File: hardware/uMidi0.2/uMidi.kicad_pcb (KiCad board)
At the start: 2 copper layers, 66 x 40.6 mm, 59 parts, among them CON1 USB-MINI-B, IC1 ATXMEGA128A4U-M, IC2 74LS14, IC3 LT1129CST-3.3, IC4 6N138, P1 MIDI In, P2 MIDI Thru, P3 MIDI T/O, P4 MIDI Out, P5 5..12 V, P6 PDI, P7 GPIO1, P8 GPIO2, P9 GPIO2

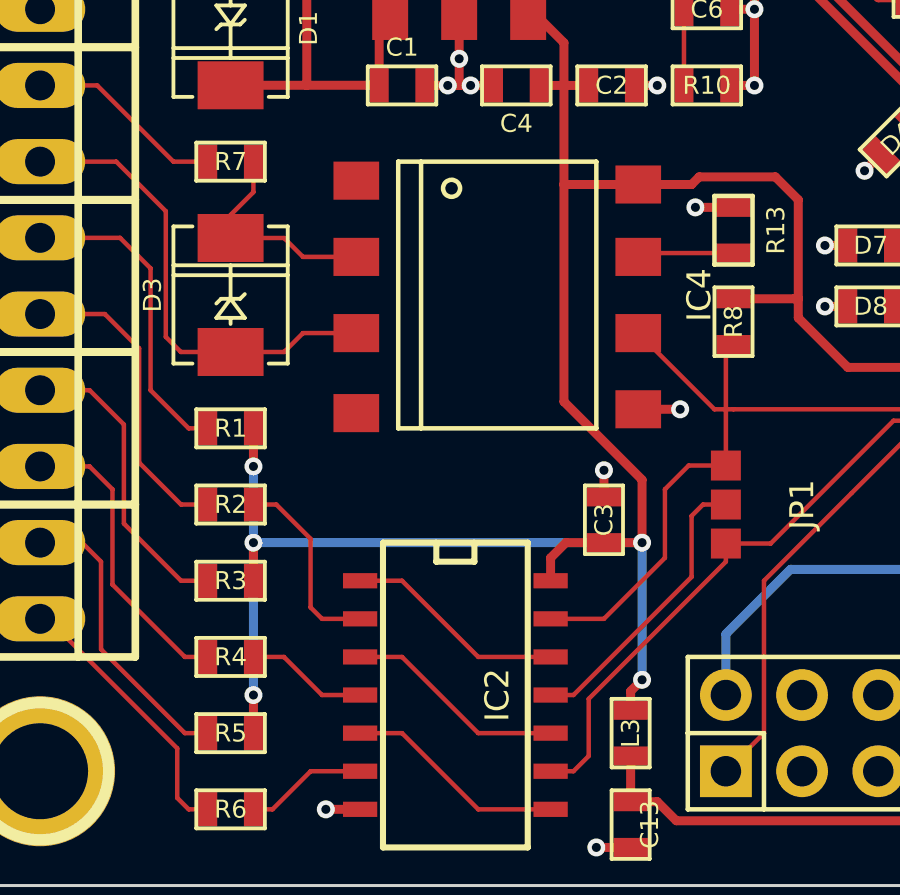
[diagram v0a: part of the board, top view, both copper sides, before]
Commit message: Modify placement of C3
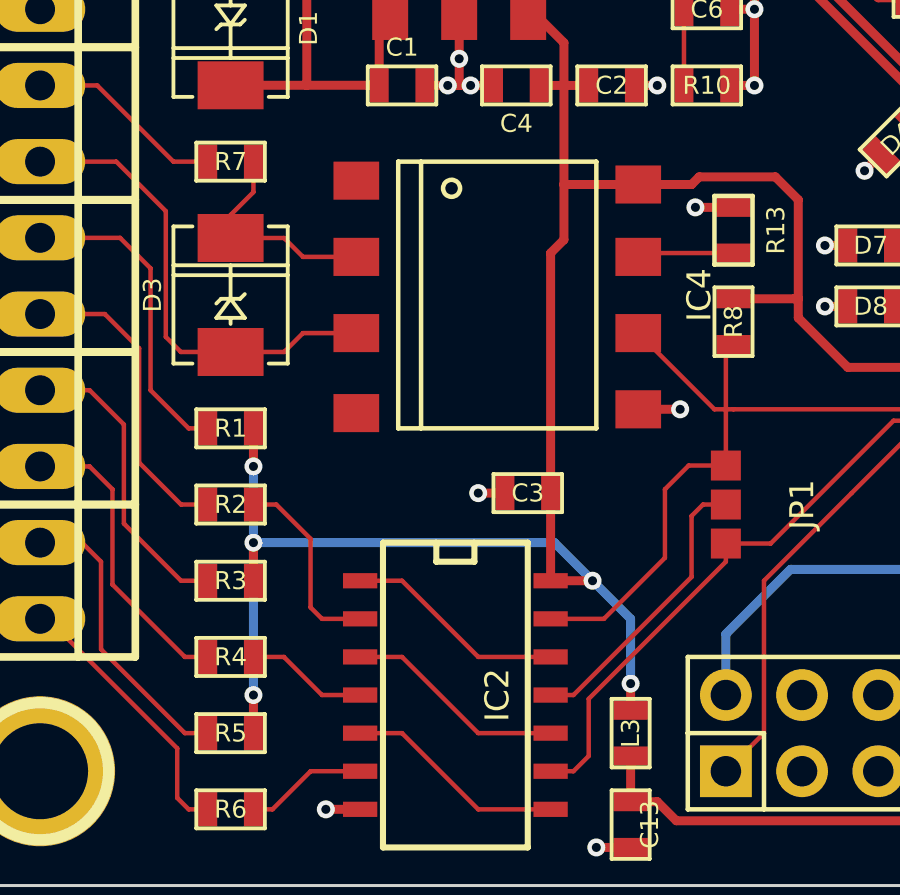
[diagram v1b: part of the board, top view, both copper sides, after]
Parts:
- moved C3 2.69 mm to (87.4, 150.7), turned to 180 degrees
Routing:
- net +3.3V: track 75.4 -> 71.2 mm
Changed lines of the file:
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@@
     (links 155)
     (no_connects 1)
-    (area 64.280952 120.39205 138.793784 166.53905)
+    (area 64.265952 120.77 137.108095 166.2406)
     (thickness 1.6)
     (drawings 4)
-    (tracks 477)
+    (tracks 475)
     (zones 0)
     (modules 59)
@@
   )
   (module SMD_Packages:SMD-0603 (layer F.Cu)
-    (at 89.916 151.638 90)
-    (attr smd)
-    (fp_text reference C3 (at 0 0 90) (layer F.SilkS)
-      (effects (font (size 0.6 0.6) (thickness 0.1143)))
-    )
-    (fp_text value 100n (at 0 0 90) (layer F.SilkS) hide
-      (effects (font (size 0.6 0.6) (thickness 0.1143)))
-    )
-    (fp_line (start -1.143 -0.635) (end 1.143 -0.635) (layer F.SilkS) (width 0.127))
-    (fp_line (start 1.143 -0.635) (end 1.143 0.635) (layer F.SilkS) (width 0.127))
-    (fp_line (start 1.143 0.635) (end -1.143 0.635) (layer F.SilkS) (width 0.127))
-    (fp_line (start -1.143 0.635) (end -1.143 -0.635) (layer F.SilkS) (width 0.127))
-    (pad 1 smd rect (at -0.762 0 90) (size 0.635 1.143) (layers F.Cu F.Paste F.Mask)
+    (at 87.376 150.749 180)
+    (attr smd)
+    (fp_text reference C3 (at 0 0 180) (layer F.SilkS)
+      (effects (font (size 0.6 0.6) (thickness 0.1143)))
+    )
+    (fp_text value 100n (at 0 0 180) (layer F.SilkS) hide
+      (effects (font (size 0.6 0.6) (thickness 0.1143)))
+    )
+    (fp_line (start -1.143 -0.635) (end 1.143 -0.635) (layer F.SilkS) (width 0.127))
+    (fp_line (start 1.143 -0.635) (end 1.143 0.635) (layer F.SilkS) (width 0.127))
+    (fp_line (start 1.143 0.635) (end -1.143 0.635) (layer F.SilkS) (width 0.127))
+    (fp_line (start -1.143 0.635) (end -1.143 -0.635) (layer F.SilkS) (width 0.127))
+    (pad 1 smd rect (at -0.762 0 180) (size 0.635 1.143) (layers F.Cu F.Paste F.Mask)
       (net 70 +3.3V))
-    (pad 2 smd rect (at 0.762 0 90) (size 0.635 1.143) (layers F.Cu F.Paste F.Mask)
+    (pad 2 smd rect (at 0.762 0 180) (size 0.635 1.143) (layers F.Cu F.Paste F.Mask)
       (net 2 GND))
     (model smd\resistors\R0603.wrl
@@
   (segment (start 82.41792 137.15492) (end 82.423 137.16) (width 0.3) (layer F.Cu) (net 1))
   (segment (start 82.588 134.747) (end 82.79 134.545) (width 0.3) (layer F.Cu) (net 1) (status 30))
+  (segment (start 86.614 150.749) (end 85.725 150.749) (width 0.3) (layer F.Cu) (net 2) (status 400000))
+  (via (at 85.725 150.749) (size 0.6) (layers F.Cu B.Cu) (net 2))
   (segment (start 90.805 162.56) (end 89.662 162.56) (width 0.3) (layer F.Cu) (net 2))
   (via (at 89.662 162.56) (size 0.6) (layers F.Cu B.Cu) (net 2))
@@
   (segment (start 89.154 128.905) (end 89.154 129.794) (width 0.3) (layer F.Cu) (net 2))
   (via (at 89.154 129.794) (size 0.6) (layers F.Cu B.Cu) (net 2))
-  (segment (start 89.916 150.876) (end 89.916 149.987) (width 0.3) (layer F.Cu) (net 2))
-  (via (at 89.916 149.987) (size 0.6) (layers F.Cu B.Cu) (net 2))
   (via (at 105.537 147.3835) (size 0.6) (layers F.Cu B.Cu) (net 2))
   (segment (start 105.537 146.558) (end 105.537 147.3835) (width 0.3) (layer F.Cu) (net 2))
@@
   (segment (start 101.092 142.494) (end 99.568 142.494) (width 0.15) (layer F.Cu) (net 68))
   (segment (start 101.092 144.526) (end 99.568 144.526) (width 0.15) (layer F.Cu) (net 69))
-  (segment (start 90.805 157.988) (end 90.805 157.353) (width 0.3) (layer F.Cu) (net 70))
-  (segment (start 91.186 156.972) (end 91.186 152.4) (width 0.3) (layer B.Cu) (net 70))
-  (via (at 91.186 156.972) (size 0.6) (layers F.Cu B.Cu) (net 70))
-  (segment (start 90.805 157.353) (end 91.186 156.972) (width 0.3) (layer F.Cu) (net 70))
-  (segment (start 89.916 152.4) (end 91.186 152.4) (width 0.3) (layer F.Cu) (net 70))
-  (segment (start 88.138 153.67) (end 88.138 152.908) (width 0.3) (layer F.Cu) (net 70))
-  (segment (start 88.646 152.4) (end 89.916 152.4) (width 0.3) (layer F.Cu) (net 70))
-  (segment (start 88.138 152.908) (end 88.646 152.4) (width 0.3) (layer F.Cu) (net 70))
+  (segment (start 89.535 153.67) (end 90.805 154.94) (width 0.3) (layer B.Cu) (net 70))
+  (segment (start 90.805 157.099) (end 90.805 157.988) (width 0.3) (layer F.Cu) (net 70) (status 800000))
+  (via (at 90.805 157.099) (size 0.6) (layers F.Cu B.Cu) (net 70))
+  (segment (start 90.805 154.94) (end 90.805 157.099) (width 0.3) (layer B.Cu) (net 70))
+  (segment (start 78.232 152.4) (end 88.265 152.4) (width 0.3) (layer B.Cu) (net 70))
+  (segment (start 89.535 153.67) (end 88.138 153.67) (width 0.3) (layer F.Cu) (net 70) (status 800000))
+  (via (at 89.535 153.67) (size 0.6) (layers F.Cu B.Cu) (net 70))
+  (segment (start 88.265 152.4) (end 89.535 153.67) (width 0.3) (layer B.Cu) (net 70))
+  (segment (start 88.138 150.749) (end 88.138 153.67) (width 0.3) (layer F.Cu) (net 70))
+  (segment (start 88.138 150.749) (end 88.138 142.748) (width 0.3) (layer F.Cu) (net 70))
+  (segment (start 88.5825 142.3035) (end 88.5825 140.462) (width 0.3) (layer F.Cu) (net 70))
+  (segment (start 88.138 142.748) (end 88.5825 142.3035) (width 0.3) (layer F.Cu) (net 70))
   (segment (start 78.232 153.67) (end 78.232 152.4) (width 0.3) (layer F.Cu) (net 70) (status 10))
   (segment (start 78.232 158.75) (end 78.232 157.48) (width 0.3) (layer F.Cu) (net 70))
@@
   (segment (start 78.232 149.86) (end 78.232 148.59) (width 0.3) (layer F.Cu) (net 70) (status 20))
   (via (at 78.232 149.86) (size 0.6) (layers F.Cu B.Cu) (net 70))
-  (via (at 91.186 152.4) (size 0.6) (layers F.Cu B.Cu) (net 70))
   (via (at 78.232 152.4) (size 0.6) (layers F.Cu B.Cu) (net 70))
   (segment (start 78.232 157.48) (end 78.232 152.4) (width 0.3) (layer B.Cu) (net 70))
   (segment (start 78.232 152.4) (end 78.232 149.86) (width 0.3) (layer B.Cu) (net 70))
-  (segment (start 91.186 152.4) (end 78.232 152.4) (width 0.3) (layer B.Cu) (net 70))
-  (segment (start 88.5825 140.462) (end 88.5825 147.701) (width 0.3) (layer F.Cu) (net 70))
   (segment (start 88.5825 137.16) (end 88.5825 140.462) (width 0.3) (layer F.Cu) (net 70))
   (segment (start 88.5825 135.7375) (end 88.5825 137.16) (width 0.3) (layer F.Cu) (net 70))
-  (segment (start 88.5825 147.701) (end 91.186 150.3045) (width 0.3) (layer F.Cu) (net 70))
-  (segment (start 91.186 150.3045) (end 91.186 152.4) (width 0.3) (layer F.Cu) (net 70))
-  (segment (start 91.186 152.4) (end 91.186 152.4) (width 0.3) (layer F.Cu) (net 70))
   (segment (start 87.39 134.545) (end 88.5825 135.7375) (width 0.3) (layer F.Cu) (net 70))
   (segment (start 88.519 137.16) (end 88.5825 137.16) (width 0.3) (layer F.Cu) (net 70))

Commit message: Placement silk screen
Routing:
- net GND: track 49.5 -> 50.4 mm, vias 25 -> 24

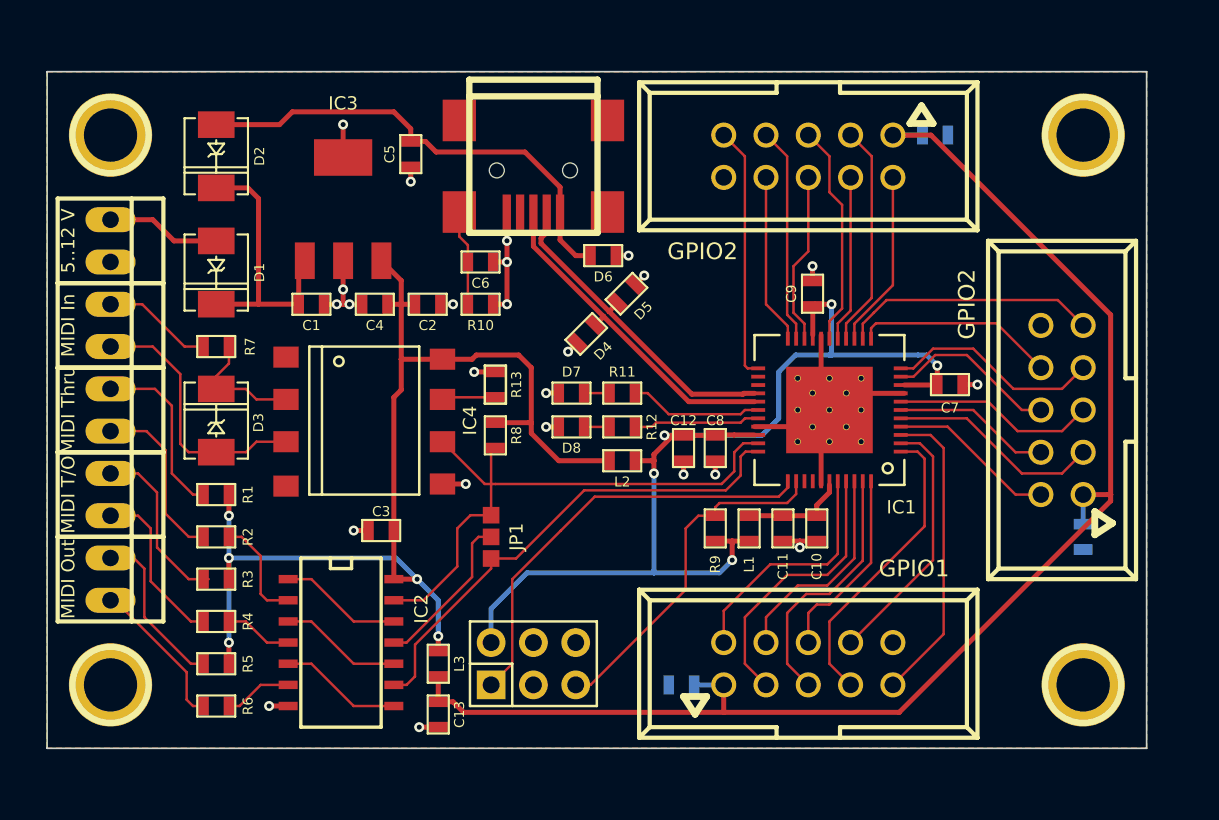
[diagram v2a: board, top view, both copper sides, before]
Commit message: Modify SMD-0603 silk screen
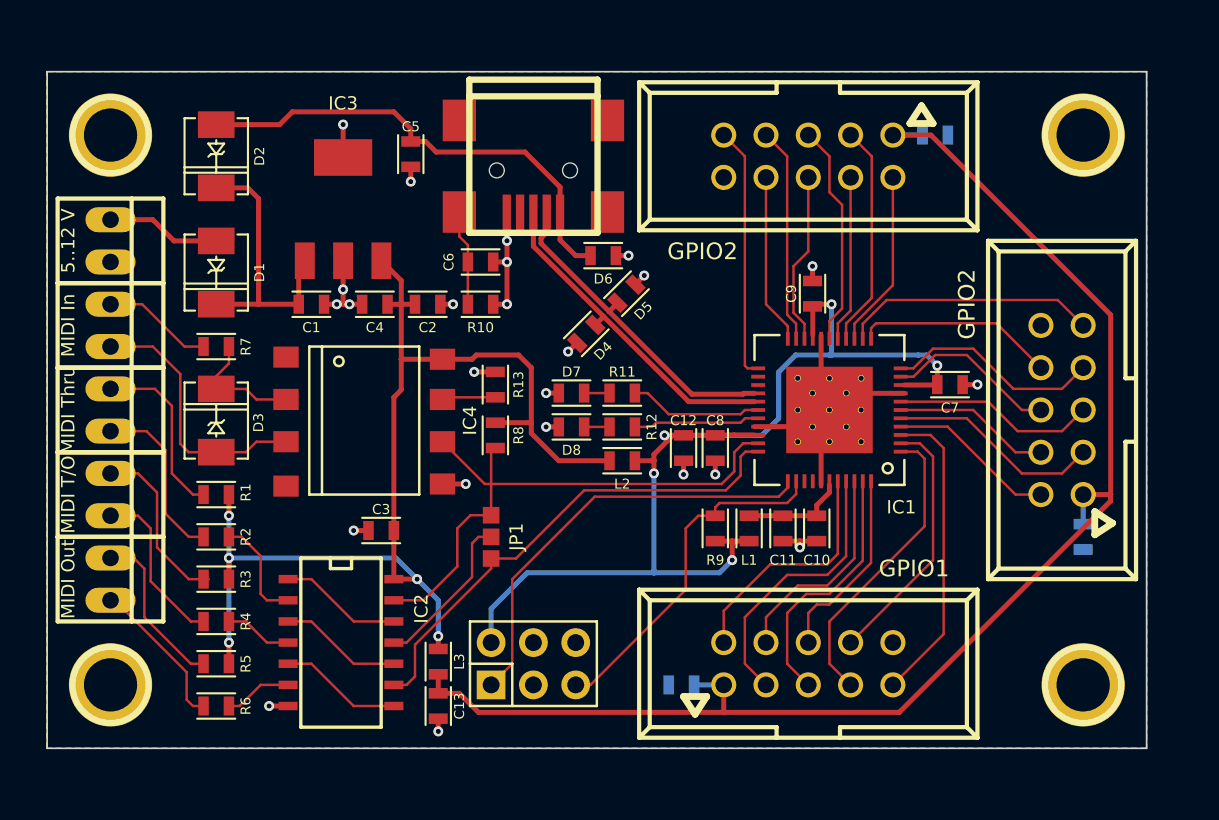
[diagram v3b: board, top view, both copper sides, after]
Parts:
- C1, C10, C11, C12, C13, C14, C15, C16, C2, C3, C4, C5, C6, C7, C8, C9, D4, D5, D6, D7, D8, L1, L2, L3, R1, R10, R11, R12, R13, R2, R3, R4, R5, R6, R7, R8, R9: footprint SMD_Packages:SMD-0603 -> SMD-0603:SMD-0603
- moved C13 0.51 mm to (90.8, 161.3)
- moved L3 0.13 mm to (90.8, 158.6)

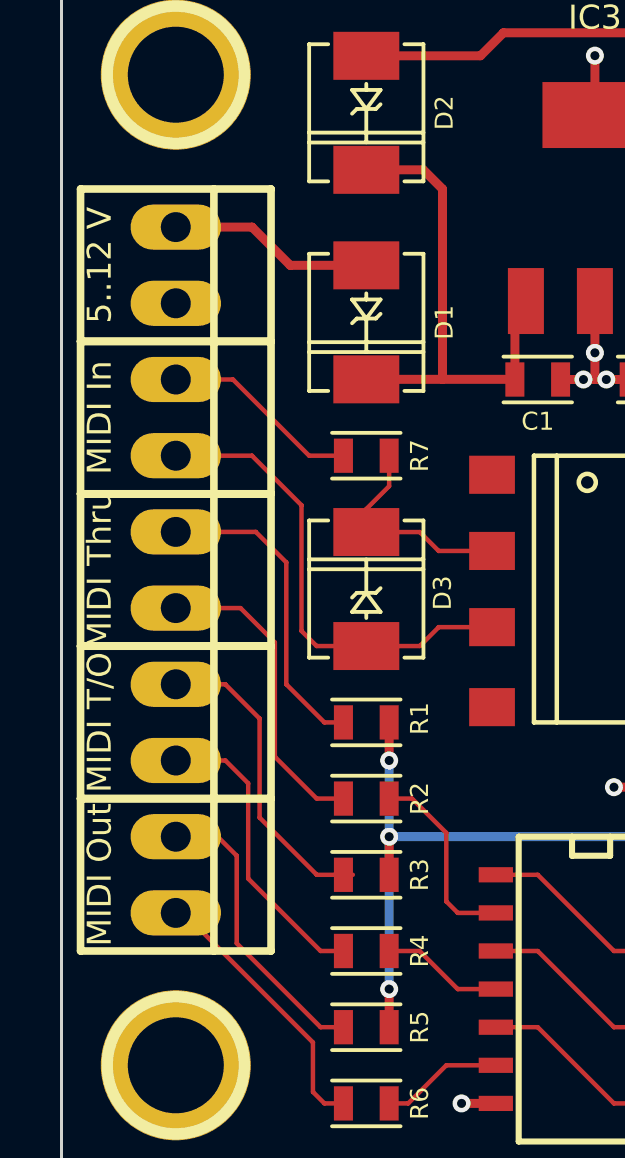
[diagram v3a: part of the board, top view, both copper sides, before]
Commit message: Label MIDI and PWR connectors
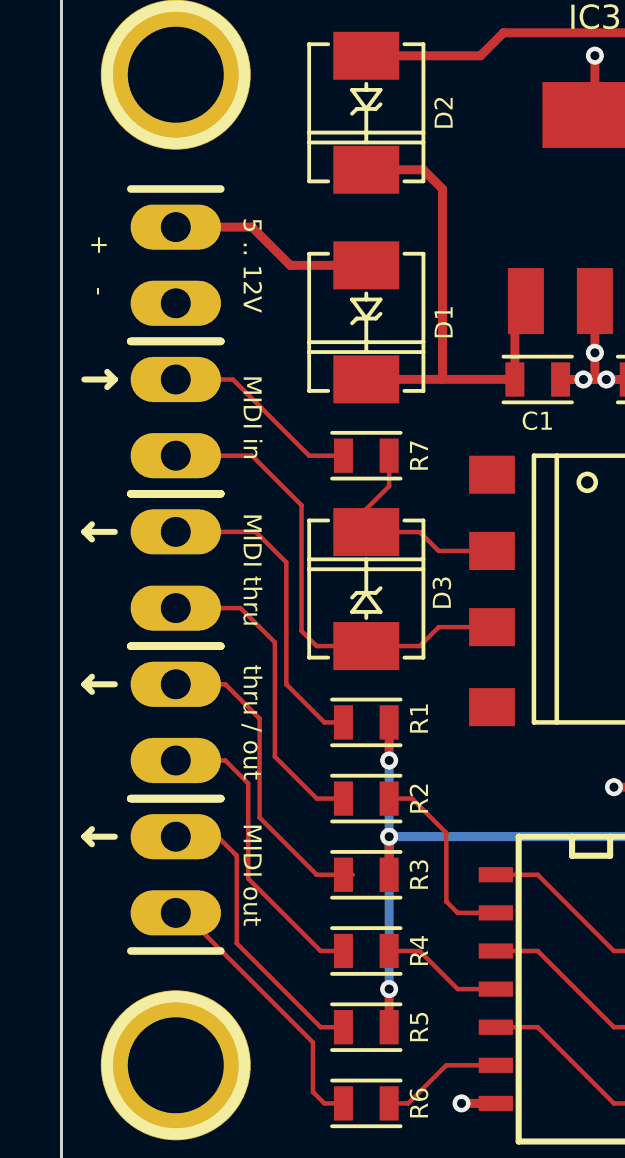
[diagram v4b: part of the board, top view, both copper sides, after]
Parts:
- P1, P2, P3, P4, P5: footprint Connect:PINHEAD1-2 -> Pinheaders:PINHEAD1-2
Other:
- board text added: "+ -"
- board text added: "5 .. 12V"
- board text added: "MIDI in"
- board text added: "MIDI out"
- board text added: "MIDI thru"
- board text added: "thru / out"
